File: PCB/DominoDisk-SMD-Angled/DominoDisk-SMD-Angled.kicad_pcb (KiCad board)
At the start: 2 copper layers, 45.7 x 38.9 mm, 32 parts, among them J1 Daisy port out, J2 ICSP_ISP6, J3 UART, J4 Daisy port in, K1 HYC77-TF09-200, U1 PC817C-S, U2 ATmega328P-AU, U3 SE5218, U4 TXB0104QPWRQ1, Y1 Crystal_GND2

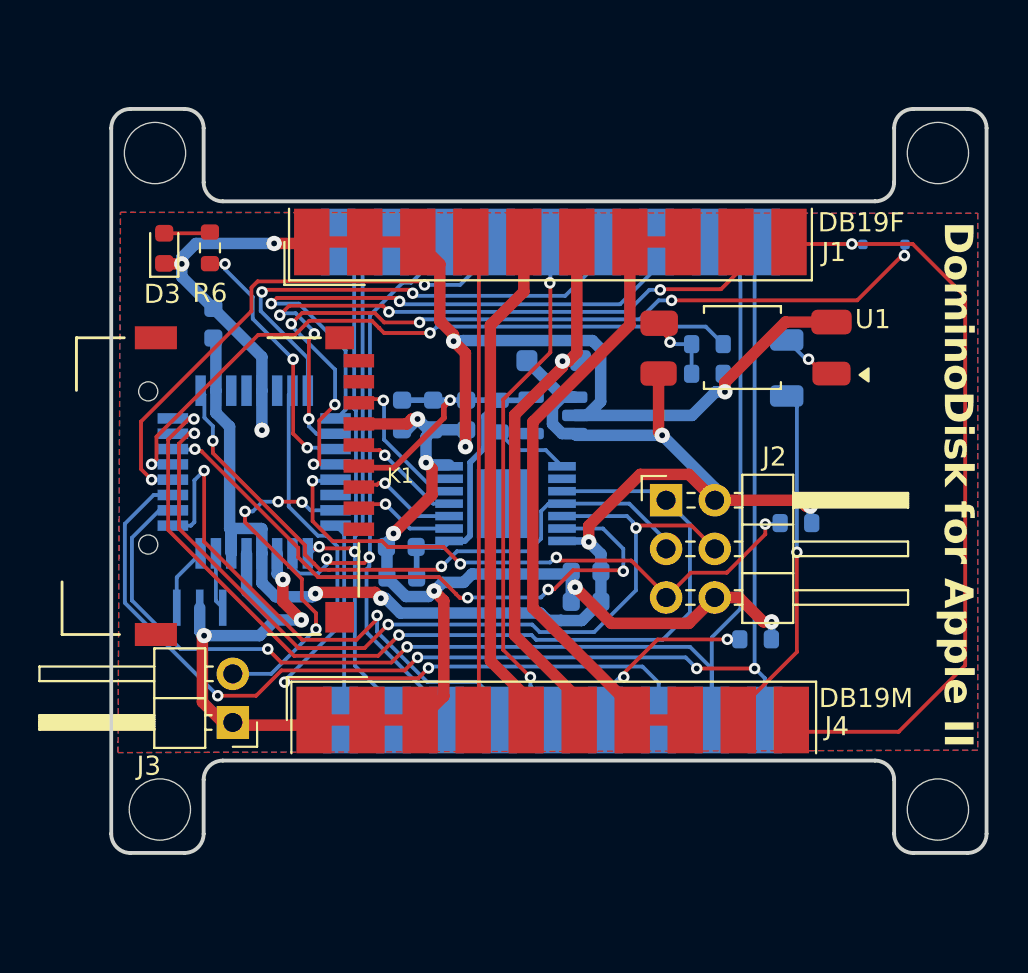
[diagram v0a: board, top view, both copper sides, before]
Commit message: Cleanup PCBs, fatter power traces
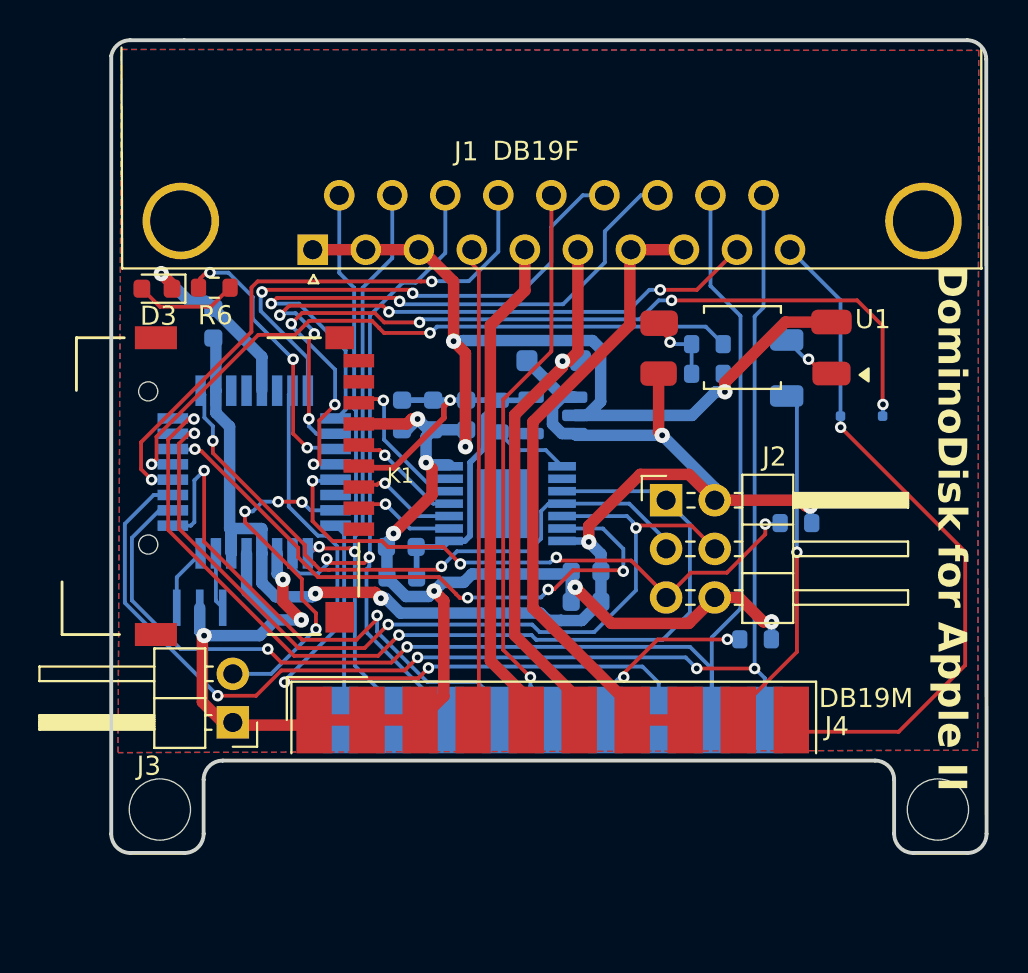
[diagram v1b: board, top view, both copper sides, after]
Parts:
- removed the REF** at (142.3, 40.0)
- removed the REF** at (101.4, 40.0)
- J1: footprint db19:DSUB-19_Female_EdgeMount_Pitch2.77mm -> DSUB-19-angled:DSUB-19_Female_Horizontal_MXS82009-8251-9246
- moved J1 12.4 mm to (109.6, 45.0)
- moved D2 9.04 mm to (138.3, 53.7)
- moved D3 2.14 mm to (101.5, 47.1), turned to 180 degrees
- moved R6 2.10 mm to (104.5, 47.0), turned to 180 degrees
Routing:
- net GND: track 145.3 -> 135.8 mm, vias 15 -> 13
- net WRPROT_out: track 40.1 -> 35.4 mm
- net Net-(D3-A): track 2.12 -> 5.40 mm
- net WRDATA: track 68.0 -> 71.1 mm
- net PH2: track 33.5 -> 36.5 mm
- net PH3_out: track 27.6 -> 30.4 mm
- net WRPROT_in: track 44.6 -> 47.1 mm
- net DRV1_out: track 29.8 -> 32.4 mm
- net HDSEL_out: track 25.0 -> 27.5 mm
- net PH1: track 29.0 -> 31.4 mm
- net WREQ: track 26.5 -> 28.9 mm, vias 2 -> 1
- net RDDATA: track 67.4 -> 69.8 mm
- net PH0: track 26.0 -> 28.4 mm
- net DRV2_out: track 35.5 -> 34.4 mm
- net LED: track 13.7 -> 14.3 mm
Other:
- board size 45.7 x 38.9 mm -> 45.7 x 42.5 mm

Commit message: Add libraries and update Domino/Angled
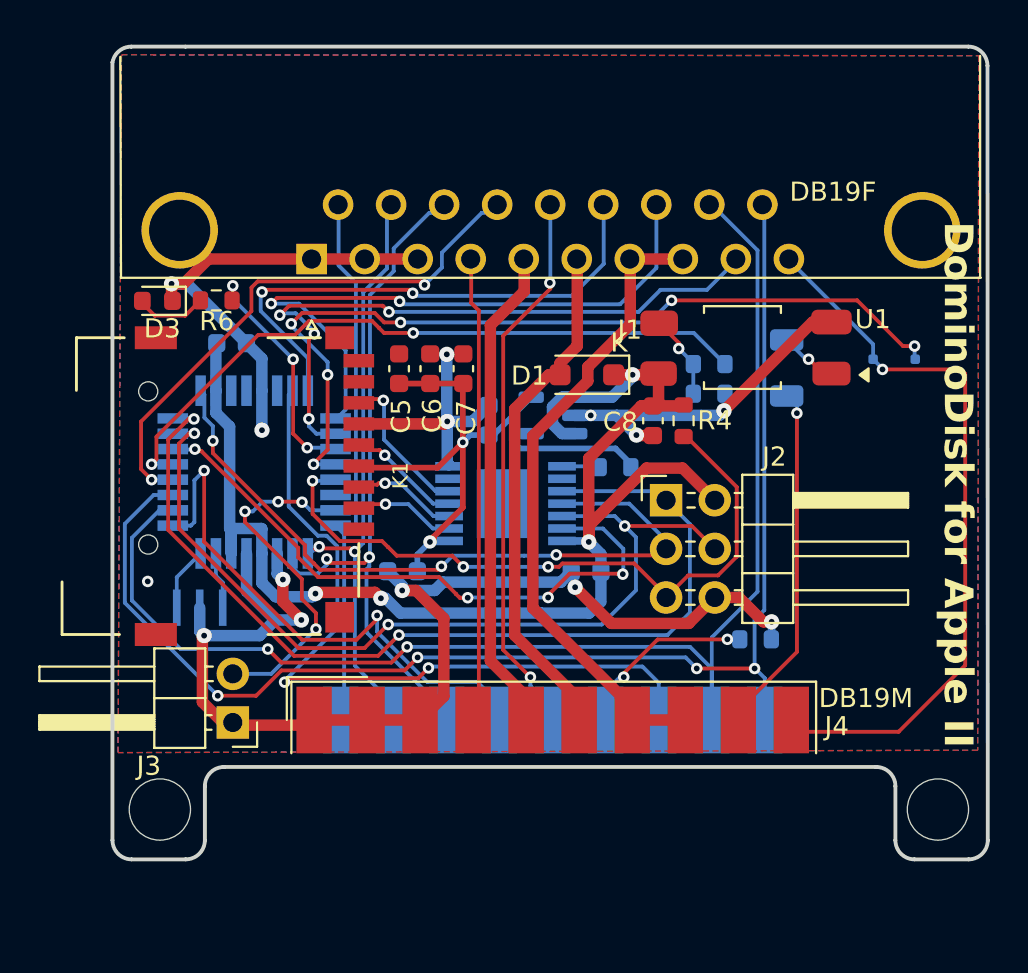
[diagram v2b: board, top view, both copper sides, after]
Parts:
- C2: value 100nF -> 100n
- C5, C6, C7, C8, D1: moved to F.Cu
- K1: footprint MICROSD-HYC77-TF09-200:MICROSD-HYC77-TF09-200 -> HYC04-TF09-200:MICROSD-HYC77-TF09-200
- R4: value 10K -> 10k; moved to F.Cu
- moved C8 10.1 mm to (127.4, 54.0), turned to 90 degrees
- moved C4 9.38 mm to (118.8, 53.9), turned to -90 degrees
- moved R4 7.94 mm to (129.0, 54.0), turned to -90 degrees
- moved R7 6.58 mm to (125.4, 56.4), turned to 180 degrees
- moved D2 3.42 mm to (140.0, 50.7)
- moved C5 2.42 mm to (114.1, 51.2), turned to -90 degrees
- moved C6 2.42 mm to (115.7, 51.2), turned to -90 degrees
- moved C7 2.42 mm to (117.5, 51.2), turned to -90 degrees
- moved D1 1.88 mm to (123.9, 51.6), turned to 180 degrees
- moved C2 1.41 mm to (105.4, 49.9), turned to 0 degrees
- moved C10 1.27 mm to (114.3, 61.8)
- moved R3 1.05 mm to (130.3, 51.0)
- moved R2 1.05 mm to (130.3, 52.6)
- moved R6 0.67 mm to (104.6, 47.7), turned to 0 degrees
- moved D3 0.64 mm to (101.5, 47.7)
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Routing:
- net GND: track 135.8 -> 119.3 mm, vias 13 -> 14
- net 3V3: track 26.4 -> 32.8 mm, vias 1 -> 2
- net RESET: track 31.3 -> 35.3 mm, vias 4 -> 3
- net SCK: track 33.1 -> 36.7 mm, vias 2 -> 3
- net 5V_burgerDisk: track 75.5 -> 72.4 mm, vias 5 -> 4
- net WRPROT_in: track 47.1 -> 44.7 mm
- net OE: track 3.96 -> 1.96 mm
- net LED: track 14.3 -> 12.3 mm
- net WRPROT_out: track 35.4 -> 37.3 mm
- net Net-(D3-A): track 5.40 -> 3.76 mm
- net PH3_out: track 30.4 -> 28.8 mm
- net 5V_apple2: track 27.4 -> 26.1 mm, vias 1 -> 0
- net PH1: track 31.4 -> 30.5 mm
- net PH0: track 28.4 -> 27.5 mm
- net WREQ: track 28.9 -> 28.0 mm, vias 1 -> 2
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
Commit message: Add logo (thanks to Javier Rivera!!)
Add my own micro/SD modules
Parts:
- added G***: LOGO, LOGO, B.Cu at (138.0, 59.8)
- U4: value TXB0104QPWRQ1 -> TXB0104PWR

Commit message: Cleanups
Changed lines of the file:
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@@
 		(tags "SOD-323F")
 		(property "Reference" "D2"
-			(at -2.6416 0 180)
+			(at -0.1778 1.5494 180)
 			(layer "B.SilkS")
 			(effects
@@
 		)
 		(fp_text user "K"
-			(at 1.651 -0.5588 0)
+			(at -2.7432 -0.5588 0)
 			(layer "B.SilkS")
 			(effects
@@
 	)
 	(segment
-		(start 110.9606 45.8516)
-		(end 110.9606 43.1046)
+		(start 111.803 59.442)
+		(end 112.1918 59.0532)
 		(width 0.2)
 		(layer "B.Cu")
@@
 	)
 	(segment
-		(start 111.8662 46.7572)
-		(end 110.9606 45.8516)
+		(start 110.803 59.442)
+		(end 111.803 59.442)
 		(width 0.2)
 		(layer "B.Cu")
@@
 	)
 	(segment
-		(start 111.803 59.442)
-		(end 111.8662 59.3788)
+		(start 111.252 59.891)
+		(end 111.252 68.9983)
 		(width 0.2)
 		(layer "B.Cu")
@@
 	)
 	(segment
-		(start 111.252 59.891)
-		(end 111.252 68.9983)
+		(start 112.1918 47.0828)
+		(end 110.9606 45.8516)
 		(width 0.2)
 		(layer "B.Cu")
@@
 	)
 	(segment
-		(start 110.803 59.442)
-		(end 111.803 59.442)
+		(start 112.1918 59.0532)
+		(end 112.1918 47.0828)
 		(width 0.2)
 		(layer "B.Cu")
@@
 	)
 	(segment
-		(start 111.8662 59.3788)
-		(end 111.8662 46.7572)
+		(start 110.9606 45.8516)
+		(end 110.9606 43.1046)
 		(width 0.2)
 		(layer "B.Cu")
@@
 	)
 	(segment
-		(start 113.4872 43.348)
-		(end 113.7306 43.1046)
+		(start 112.5982 46.89745)
+		(end 113.4872 46.00845)
 		(width 0.2)
 		(layer "B.Cu")
@@
 	)
 	(segment
+		(start 111.802 60.7988)
+		(end 112.5982 60.0026)
+		(width 0.2)
+		(layer "B.Cu")
+		(net 4)
+	)
+	(segment
 		(start 111.8108 66.753633)
 		(end 113.8336 68.776433)
@@
 	)
 	(segment
-		(start 111.802 60.7988)
-		(end 112.2472 60.3536)
+		(start 113.4872 46.00845)
+		(end 113.4872 43.348)
 		(width 0.2)
 		(layer "B.Cu")
@@
 	)
 	(segment
-		(start 112.2472 47.24845)
-		(end 113.4872 46.00845)
-		(width 0.2)
-		(layer "B.Cu")
-		(net 4)
-	)
-	(segment
-		(start 112.2472 60.3536)
-		(end 112.2472 47.24845)
+		(start 112.5982 60.0026)
+		(end 112.5982 46.89745)
 		(width 0.2)
 		(layer "B.Cu")
@@
 	)
 	(segment
-		(start 113.4872 46.00845)
-		(end 113.4872 43.348)
+		(start 109.785637 60.588471)
+		(end 109.482108 60.892)
 		(width 0.2)
 		(layer "B.Cu")
@@
 	)
 	(segment
-		(start 109.785637 60.588471)
-		(end 109.482108 60.892)
+		(start 113.4872 43.348)
+		(end 113.7306 43.1046)
 		(width 0.2)
 		(layer "B.Cu")
@@
 	)
 	(segment
-		(start 112.5982 47.393838)
-		(end 113.8382 46.153838)
+		(start 110.3464 61.4756)
+		(end 109.879 61.943)
 		(width 0.2)
 		(layer "B.Cu")
@@
 	)
 	(segment
-		(start 110.3464 61.4756)
-		(end 109.879 61.943)
+		(start 109.879 61.943)
+		(end 108.8802 61.943)
 		(width 0.2)
 		(layer "B.Cu")
@@
 	)
 	(segment
-		(start 109.879 61.943)
-		(end 108.8802 61.943)
+		(start 113.8382 44.9626)
+		(end 115.6962 43.1046)
 		(width 0.2)
 		(layer "B.Cu")
@@
 	)
 	(segment
-		(start 115.6962 43.1046)
-		(end 116.5006 43.1046)
+		(start 113.03 46.962038)
+		(end 113.8382 46.153838)
 		(width 0.2)
 		(layer "B.Cu")
@@
 	)
 	(segment
-		(start 112.5982 61.059377)
-		(end 112.5982 47.393838)
+		(start 113.8382 46.153838)
+		(end 113.8382 44.9626)
 		(width 0.2)
 		(layer "B.Cu")
@@
 	)
 	(segment
-		(start 110.3464 61.1798)
-		(end 110.3464 61.4756)
+		(start 115.6962 43.1046)
+		(end 116.5006 43.1046)
 		(width 0.2)
 		(layer "B.Cu")
@@
 	)
 	(segment
-		(start 112.4202 65.014367)
-		(end 116.6036 69.197767)
+		(start 112.566472 61.091105)
+		(end 113.03 60.627577)
 		(width 0.2)
 		(layer "B.Cu")
@@
 	)
 	(segment
-		(start 113.8382 44.9626)
-		(end 115.6962 43.1046)
+		(start 110.3464 61.1798)
+		(end 110.3464 61.4756)
 		(width 0.2)
 		(layer "B.Cu")
@@
 	)
 	(segment
-		(start 112.566472 61.575928)
-		(end 112.4202 61.7222)
+		(start 112.4202 65.014367)
+		(end 116.6036 69.197767)
 		(width 0.2)
 		(layer "B.Cu")
@@
 	)
 	(segment
-		(start 112.566472 61.091105)
-		(end 112.566472 61.575928)
+		(start 112.566472 61.575928)
+		(end 112.4202 61.7222)
 		(width 0.2)
 		(layer "B.Cu")
@@
 	(segment
 		(start 112.566472 61.091105)
-		(end 112.5982 61.059377)
+		(end 112.566472 61.575928)
 		(width 0.2)
 		(layer "B.Cu")
@@
 	)
 	(segment
-		(start 113.8382 46.153838)
-		(end 113.8382 44.9626)
+		(start 113.03 60.627577)
+		(end 113.03 46.962038)
 		(width 0.2)
 		(layer "B.Cu")
@@
 	)
 	(segment
-		(start 113.411 58.3184)
+		(start 113.9444 58.3184)
 		(end 112.0354 58.3184)
 		(width 0.2)
@@
 	)
 	(via
-		(at 113.411 58.3184)
+		(at 113.9444 58.3184)
 		(size 0.6)
 		(drill 0.3)
@@
 	)
 	(segment
-		(start 115.8794 59.593)
-		(end 116.7312 59.593)
+		(start 113.9444 58.3184)
+		(end 114.6048 58.3184)
 		(width 0.2)
 		(layer "B.Cu")
@@
 	)
 	(segment
-		(start 113.411 58.3184)
-		(end 114.6048 58.3184)
+		(start 114.6048 58.3184)
+		(end 115.8794 59.593)
 		(width 0.2)
 		(layer "B.Cu")
@@
 	)
 	(segment
-		(start 114.6048 58.3184)
-		(end 115.8794 59.593)
+		(start 115.8794 59.593)
+		(end 116.7312 59.593)
 		(width 0.2)
 		(layer "B.Cu")
@@
 	)
 	(segment
-		(start 112.9792 57.3024)
-		(end 112.1194 57.3024)
+		(start 113.0554 57.2262)
+		(end 112.9792 57.3024)
 		(width 0.2)
 		(layer "F.Cu")
@@
 	)
 	(segment
-		(start 113.3856 57.2262)
+		(start 113.9444 57.2262)
 		(end 113.0554 57.2262)
 		(width 0.2)
@@
 	)
 	(segment
-		(start 113.0554 57.2262)
-		(end 112.9792 57.3024)
+		(start 112.9792 57.3024)
+		(end 112.1194 57.3024)
 		(width 0.2)
 		(layer "F.Cu")
@@
 	)
 	(via
-		(at 113.3856 57.2262)
+		(at 113.9444 57.2262)
 		(size 0.6)
 		(drill 0.3)
@@
 	)
 	(segment
-		(start 113.3856 57.2262)
+		(start 113.9444 57.2262)
 		(end 114.1984 57.2262)
 		(width 0.2)
@@
 	)
 	(segment
-		(start 113.2996 52.896399)
-		(end 113.2996 52.846399)
+		(start 112.017 53.0286)
+		(end 113.885 53.0286)
 		(width 0.2)
 		(layer "F.Cu")
@@
 	)
 	(segment
-		(start 113.285201 52.832)
-		(end 112.049 52.832)
+		(start 113.9444 52.9692)
+		(end 113.821599 52.846399)
 		(width 0.2)
 		(layer "F.Cu")
@@
 	)
 	(segment
-		(start 113.2996 52.846399)
-		(end 113.285201 52.832)
+		(start 113.885 53.0286)
+		(end 113.9444 52.9692)
 		(width 0.2)
 		(layer "F.Cu")
@@
 	)
 	(via
-		(at 113.2996 52.896399)
+		(at 113.9444 52.9692)
 		(size 0.6)
 		(drill 0.3)
@@
 	)
 	(segment
-		(start 116.0292 57.643)
-		(end 116.7312 57.643)
-		(width 0.2)
-		(layer "B.Cu")
-		(net 43)
-	)
-	(segment
-		(start 113.32 52.896399)
-		(end 113.3348 52.911199)
+		(start 114.5032 56.117)
+		(end 116.0292 57.643)
 		(width 0.2)
 		(layer "B.Cu")
@@
 	)
 	(segment
-		(start 113.3348 52.911199)
-		(end 113.3348 54.9486)
+		(start 114.5032 53.528)
+		(end 114.5032 56.117)
 		(width 0.2)
 		(layer "B.Cu")
@@
 	)
 	(segment
-		(start 113.2996 52.896399)
-		(end 113.32 52.896399)
+		(start 113.9444 52.9692)
+		(end 114.5032 53.528)
 		(width 0.2)
 		(layer "B.Cu")
@@
 	)
 	(segment
-		(start 113.3348 54.9486)
-		(end 116.0292 57.643)
+		(start 116.0292 57.643)
+		(end 116.7312 57.643)
 		(width 0.2)
 		(layer "B.Cu")
@@
 	)
 	(segment
-		(start 113.373491 55.765109)
+		(start 113.9444 55.6514)
+		(end 113.259782 55.6514)
+		(width 0.2)
+		(layer "F.Cu")
+		(net 44)
+	)
+	(segment
+		(start 113.259782 55.6514)
 		(end 113.107382 55.499)
 		(width 0.2)
@@
 	)
 	(via
-		(at 113.373491 55.765109)
+		(at 113.9444 55.6514)
 		(size 0.6)
 		(drill 0.3)
@@
 	)
 	(segment
-		(start 113.373491 55.765109)
+		(start 113.9444 56.336018)
 		(end 115.901382 58.293)
 		(width 0.2)
 		(layer "B.Cu")
+		(net 44)
+	)
+	(segment
+		(start 113.9444 55.6514)
+		(end 113.9444 56.336018)
+		(width 0.2)
+		(layer "B.Cu")

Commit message: Update from -SMD
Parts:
- C8: moved to B.Cu
- R6: value 150 -> 100
- Y1: value Crystal_GND2 -> Resonator
- moved C2 13.5 mm to (107.3, 63.3), turned to 180 degrees
- moved R7 6.63 mm to (119.4, 53.7), turned to -90 degrees
- moved C7 4.06 mm to (117.0, 55.3)
- moved C5 4.05 mm to (114.0, 55.3)
- moved C6 4.05 mm to (115.5, 55.3)
- moved D2 2.93 mm to (137.1, 51.3), turned to 90 degrees
- moved D3 2.17 mm to (103.7, 47.9), turned to 90 degrees
- moved C8 2.04 mm to (125.3, 53.7)
- moved C4 0.98 mm to (117.9, 53.7)
- moved R6 0.82 mm to (105.4, 47.9), turned to 90 degrees
- moved J1 0.49 mm to (109.2, 45.2)
- moved G*** 0.22 mm to (138.1, 60.0)
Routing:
- net 3V3: track 32.8 -> 21.2 mm, vias 2 -> 1
- net WRPROT_out: track 37.3 -> 26.7 mm
- net GND: track 119.3 -> 127.4 mm, vias 14 -> 13
- net CS: track 32.9 -> 38.8 mm
- net SCK: track 36.7 -> 42.0 mm
- net TX: track 18.1 -> 13.0 mm, vias 4 -> 2
- net PH3_in: track 28.4 -> 23.6 mm
- net 5V_burgerDisk: track 72.4 -> 68.6 mm, vias 4 -> 5
- net RDDATA: track 70.2 -> 67.5 mm
- net OE: track 1.96 -> 4.05 mm
- net Net-(D3-A): track 3.76 -> 2.31 mm
- net PH3_out: track 28.8 -> 30.3 mm
- net -12V: track 24.4 -> 25.7 mm
- net MOSI: track 46.6 -> 47.7 mm
- net PH2: track 35.7 -> 36.7 mm
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
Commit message: Update details
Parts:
- removed the C5 at (114.0, 55.3)
- removed the C6 at (115.5, 55.3)
- C1: renamed from C7; value 100n -> 22uF; footprint Capacitor_SMD:C_0603_1608Metric -> Capacitor_SMD:C_0805_2012Metric; moved to B.Cu
- C4: renamed from C2; moved to F.Cu
- J4: renamed from J3; footprint Connector_PinHeader_2.54mm:PinHeader_1x02_P2.54mm_Horizontal -> Connector_PinHeader_2.54mm:PinHeader_1x02_P2.54mm_Vertical
- K1: value HYC77-TF09-200 -> TF-104 MicroSD card holder; footprint HYC04-TF09-200:MICROSD-HYC77-TF09-200 -> TF-104:TF-SMD_TF-104
- R2: renamed from R1; moved to F.Cu
- REF**3, REF**4: renamed from REF**; value MountingHole_3.2mm_M3 -> MountingHole_2.5mm; footprint MountingHole:MountingHole_3.2mm_M3 -> MountingHole:MountingHole_2.5mm
- U3: renamed from U4; value TXB0104PWR -> TXB0104PWR level shifter
- U4: renamed from U3; value SE5218 -> SE5218ALG voltage regulator
- Y1: value Resonator -> CSTNE16M0V530000R0 Resonator
- moved D1 35.5 mm to (139.0, 51.3), turned to 0 degrees
- moved R1 33.6 mm to (138.9, 49.7), turned to 180 degrees
- moved R6 19.2 mm to (112.4, 59.7), turned to 90 degrees
- moved R5 18.8 mm to (112.4, 56.6), turned to -90 degrees
- moved C5 17.1 mm to (109.4, 60.0)
- moved U4 16.8 mm to (106.6, 60.0)
- moved C2 15.9 mm to (108.6, 57.5)
- moved C6 15.5 mm to (103.7, 59.9), turned to 90 degrees
- moved C1 14.6 mm to (102.5, 54.5)
- moved U3 13.0 mm to (107.5, 53.9)
- moved C4 12.9 mm to (119.1, 58.0), turned to 0 degrees
- moved Y1 12.5 mm to (115.9, 61.1)
- moved U2 12.4 mm to (118.7, 54.5)
- moved R4 10.8 mm to (109.1, 50.3), turned to 0 degrees
- moved R7 10.2 mm to (125.5, 58.2), turned to -90 degrees
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- renumbered C9 to C2, C10 to C3, C8 to C5, C4 to C6, D3 to D1, D1 to D2, D2 to D3, J4 to J3, R6 to R1, R4 to R3, R7 to R4, R3 to R5, R2 to R6, R5 to R7
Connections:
- K1 pad 9: (no net) -> GND
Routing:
- net GND: track 127.4 -> 41.2 mm, vias 13 -> 8
- net CS: track 38.8 -> 4.86 mm, vias 4 -> 0
- net WRPROT_in: track 45.0 -> 11.7 mm, vias 6 -> 0
- net DRV2_burgerDisk: track 35.6 -> 2.81 mm, vias 2 -> 0
- net WRDATA: track 71.0 -> 41.9 mm, vias 4 -> 2
- net MISO: track 51.0 -> 21.9 mm, vias 2 -> 1
- net RDDATA: track 67.5 -> 39.7 mm
- net DRV1_out: track 32.8 -> 9.31 mm, vias 2 -> 0
- net MOSI: track 47.7 -> 25.3 mm, vias 3 -> 1
- net DRV2_out: track 33.8 -> 11.9 mm, vias 5 -> 0
- net DRV1_in: track 40.6 -> 19.7 mm, vias 4 -> 2
- net RESET: track 34.9 -> 14.4 mm, vias 3 -> 1
- net HDSEL_out: track 27.7 -> 7.85 mm, vias 2 -> 0
- net PH3_out: track 30.3 -> 13.2 mm, vias 2 -> 1
- net SCK: track 42.0 -> 25.2 mm, vias 3 -> 2
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- added copper zone on In1.Cu, net GND
- added copper zone on In2.Cu, net GND
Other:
- board size 45.7 x 42.5 mm -> 45 x 35.2 mm
- copper layers 2 -> 4
- board text added: "C. Leroy-Mira www.colino.net"
- board text added: "DominoDisk"
- board text added: "TX/GND"
- board text removed: "DominoDisk for Apple II"
